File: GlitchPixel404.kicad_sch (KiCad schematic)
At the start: 61 parts, among them J1 USB_C_Receptacle_USB2.0_16P, J2 VOLTLINK, J5 Barrel_Jack_Switch, J7 Output, Q1 AONR21357-ES, Q2 MMBT3904, SW1 Reset, SW2 Boot, SW3 SW_SP3T, SW4 USER, U1 ESP32-PICO-MINI-02U-N8R2, U2 TPS54202DDC, U3 CH224K, U4 CH340N, U5 IRM-H6xxT, U6 74LVC2G34, U7 HE2021A50HMR, U8 74LVC2G34

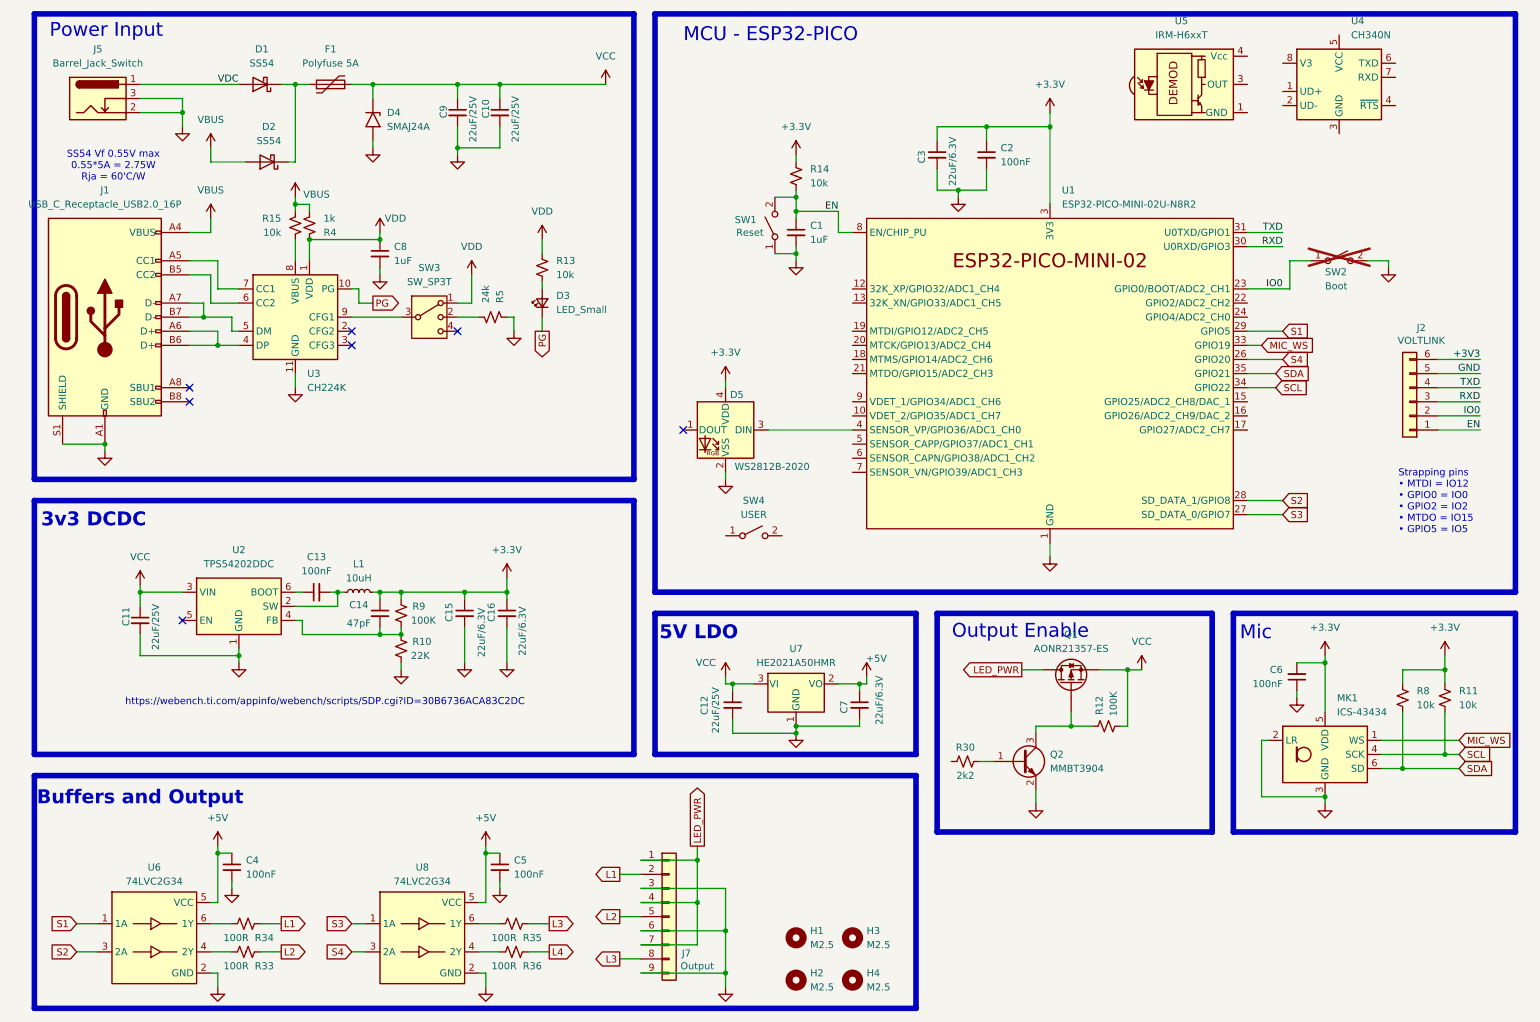
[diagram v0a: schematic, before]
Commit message: Added fet protection and started layout
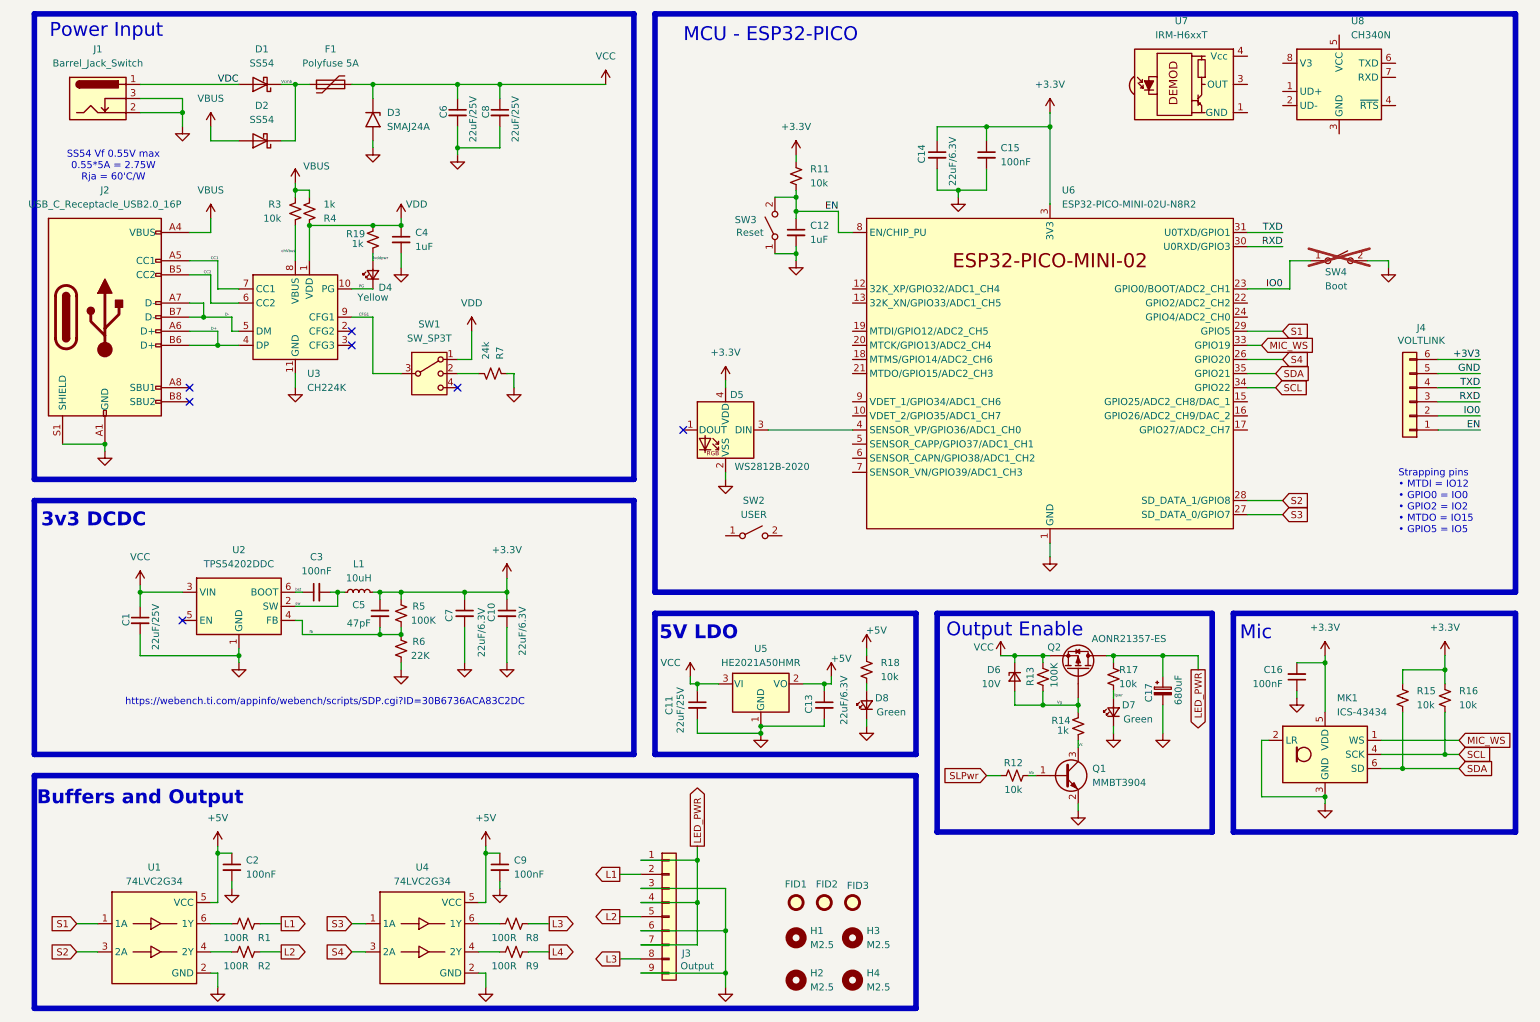
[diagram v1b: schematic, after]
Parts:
- removed R13: 10k, Resistor_SMD:R_0402_1005Metric, symbol Device:R_Small_US
- removed R30: 2k2, Resistor_SMD:R_0603_1608Metric, symbol Device:R_Small_US
- added C17: 680uF, Capacitor_SMD:CP_Elec_10x12.5, symbol Device:C_Polarized_Small
- added D6: 10V, Diode_SMD:D_SOD-123, symbol Device:D_Zener_Small
- added D7, D8: Green, LED_SMD:LED_0603_1608Metric, symbol Device:LED_Small
- added FID1, FID2, FID3: Fiducial, Fiducial:Fiducial_1mm_Mask2mm, symbol Mechanical:Fiducial
- added R12, R17, R18: 10k, Resistor_SMD:R_0402_1005Metric, symbol Device:R_Small_US
- added R14, R19: 1k, Resistor_SMD:R_0402_1005Metric, symbol Device:R_Small_US
- D4: renamed from D3; value LED_Small -> Yellow; LCSC (none) -> C72038; MPN (none) -> 19-213/Y2C-CQ2R2L/3T(CY)
- renumbered C11 to C1, C16 to C10, C12 to C11, C1 to C12, C7 to C13, C3 to C14, C2 to C15, C6 to C16, C4 to C2, C13 to C3, C8 to C4, C14 to C5, C9 to C6, C15 to C7, C10 to C8, C5 to C9, D4 to D3, J5 to J1, J1 to J2, J7 to J3, J2 to J4, Q2 to Q1, Q1 to Q2, R34 to R1, R14 to R11, R12 to R13, R8 to R15, R11 to R16, R33 to R2, R15 to R3, R9 to R5, R10 to R6, R5 to R7, R35 to R8, R36 to R9, SW3 to SW1, SW4 to SW2, SW1 to SW3, SW2 to SW4, U6 to U1, U8 to U4, U7 to U5, U1 to U6, U5 to U7, U4 to U8
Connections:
- net +5V: now also R18.1
- net GND: now also C17.2, D7.1 (K), D8.1 (K)
- net LED_PWR: now also C17.1, R17.1
- net VCC: now also D6.1 (K)
- net VDD: now also R19.2
- net Vg: now reaches Q2.G, R13.1
- net Vg: now also D6.2 (A), R14.2; no longer Q1.3 (C)
- net lvddpwr: now reaches D4.2 (A)
- net lvddpwr: now also R19.1
- net fb: now reaches C5.2, R5.2, R6.1, U2.4 (FB)
- net sw: now reaches C3.2, L1.1, U2.2 (SW)
- net bst: now reaches C3.1, U2.6 (BOOT)
- net CC1: now reaches J2.A5 (CC1), U3.7 (CC1)
- net D+: now reaches J2.A6 (D+), J2.B6 (D+), U3.4 (DP)
- net D-: now reaches J2.A7 (D-), J2.B7 (D-), U3.5 (DM)
- net CC2: now reaches J2.B5 (CC2), U3.6 (CC2)
- net Vb: now reaches Q1.1 (B)
- net Vb: now also R12.2
- net CFG1: now reaches SW1.3, U3.9 (CFG1)
- net Vcmb: now reaches D1.1 (K), D2.1 (K), F1.1
- net chVbus: now reaches R3.2, U3.8 (VBUS)
- new net: D8.2 (A), R18.2
- new net SLPwr: R12.1
- new net Vc: Q1.3 (C), R14.1
- new net llpwr: D7.2 (A), R17.2
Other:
- moved on the sheet: C11, C13, C4, D2, D4, Q1, Q2, R13, R3, R4, R7, SW1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

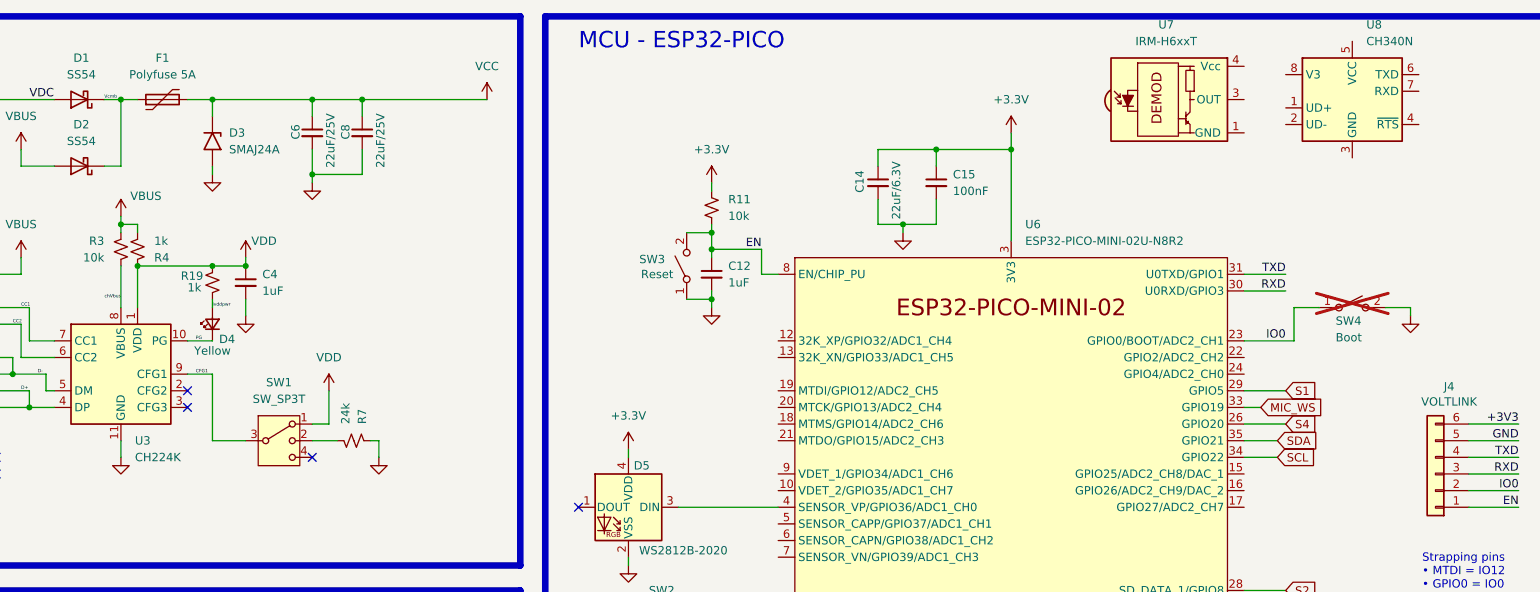
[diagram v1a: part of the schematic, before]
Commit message: remove CH340 and start layout
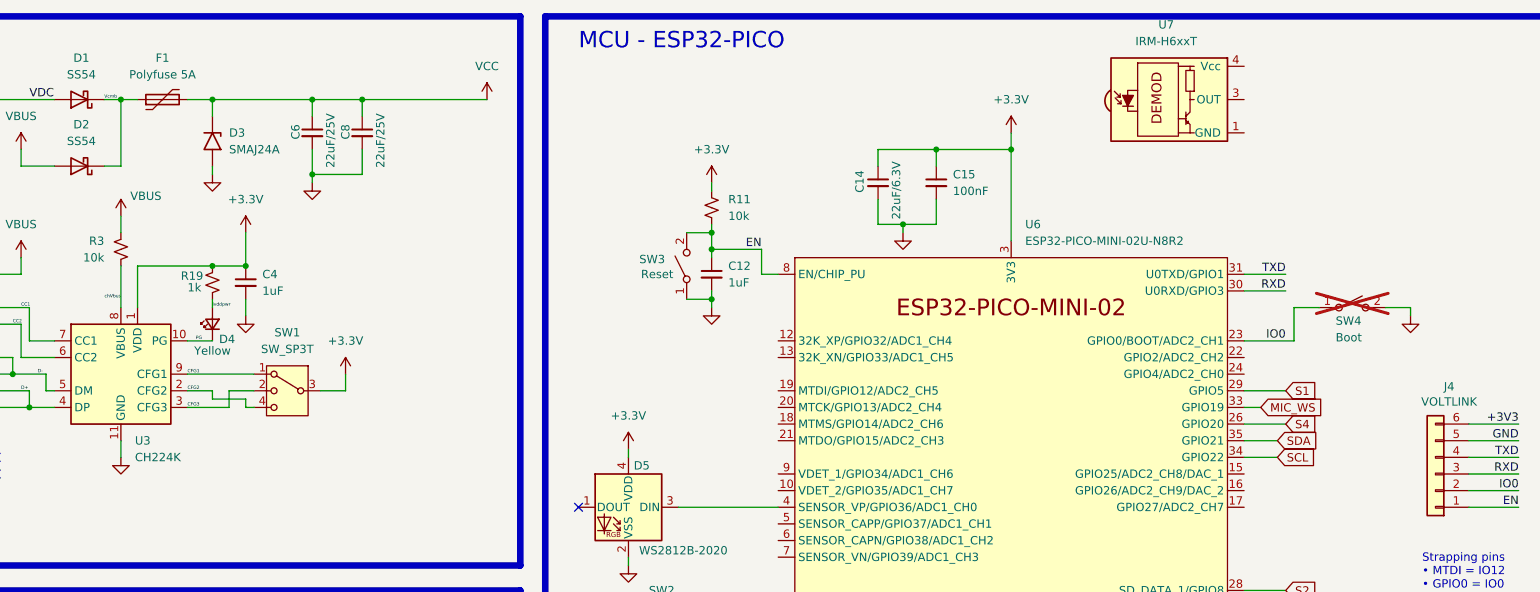
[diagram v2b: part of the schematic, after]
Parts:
- removed R4: 1k, Resistor_SMD:R_0402_1005Metric, symbol Device:R_Small_US
- removed R7: 24k, Resistor_SMD:R_0603_1608Metric, symbol Device:R_Small_US
- removed U8: CH340N, Package_SO:SOP-8_3.9x4.9mm_P1.27mm, symbol Interface_USB:CH340N
- SW4: now in the parts list
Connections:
- net +3.3V: now also C4.1, R19.2, SW1.3, U3.1 (VDD)
- net CFG1: now also SW1.1; no longer SW1.3
- net CFG3: now reaches SW1.2
- net CFG3: now also U3.3 (CFG3)
- net CFG2: now reaches SW1.4
- net CFG2: now also U3.2 (CFG2)
- removed net VDD: C4.1, R19.2, SW1.1, U3.1 (VDD)
- no-connect marks 7 -> 4
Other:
- moved on the sheet: SW1

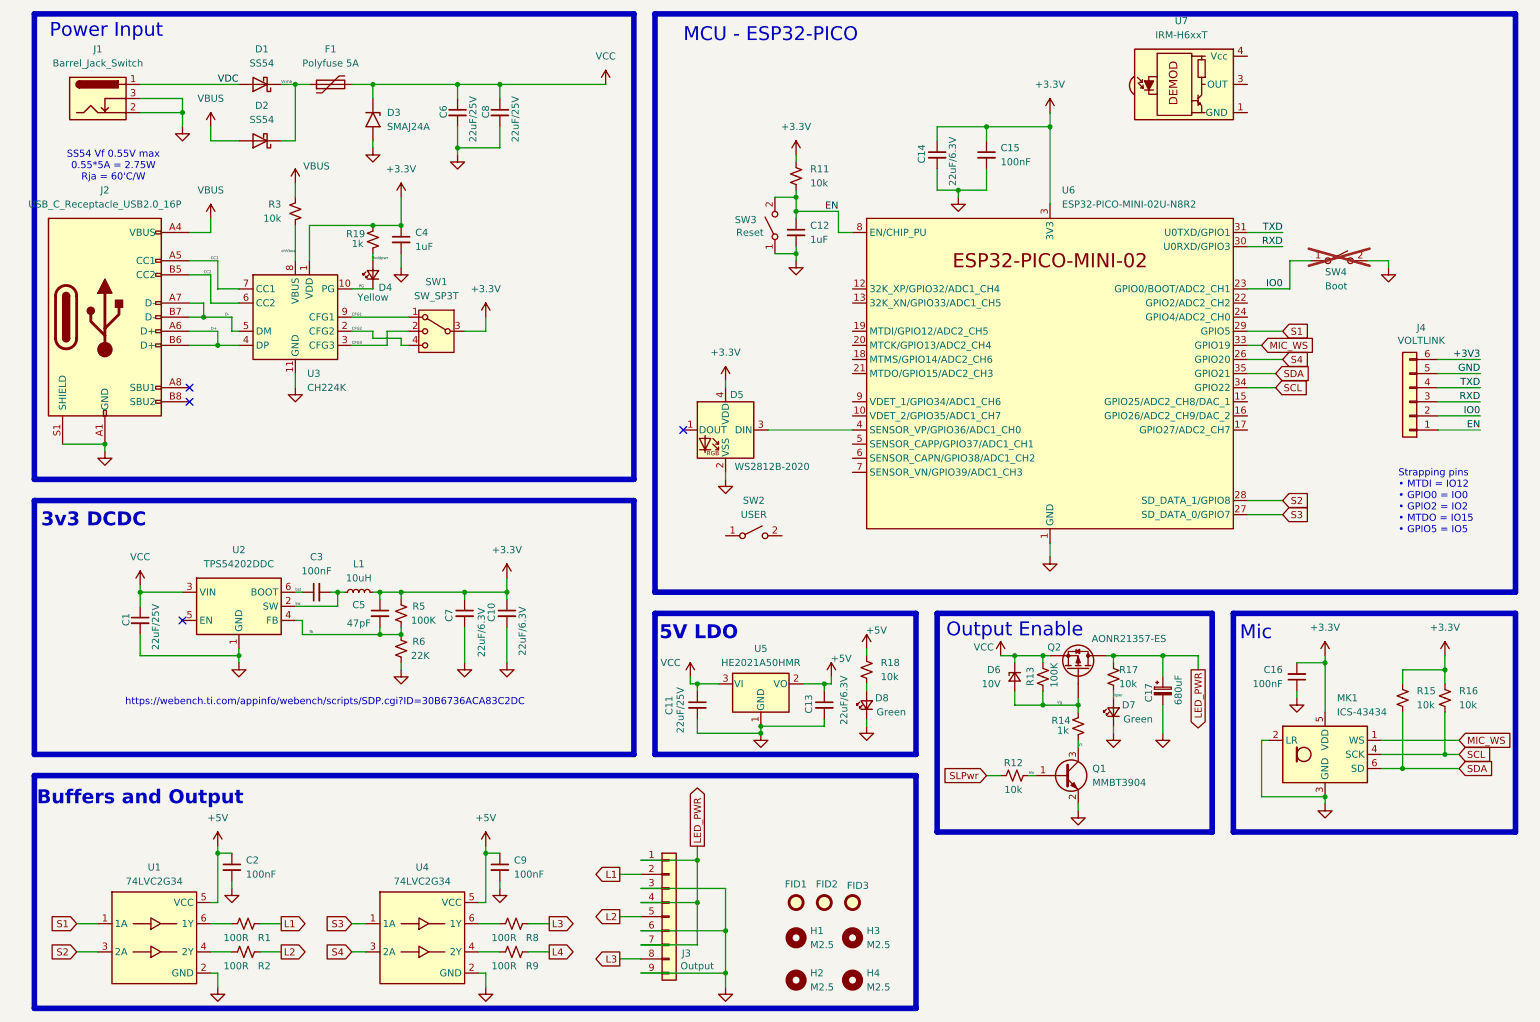
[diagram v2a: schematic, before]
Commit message: Layout 80% complete, some circuit changes
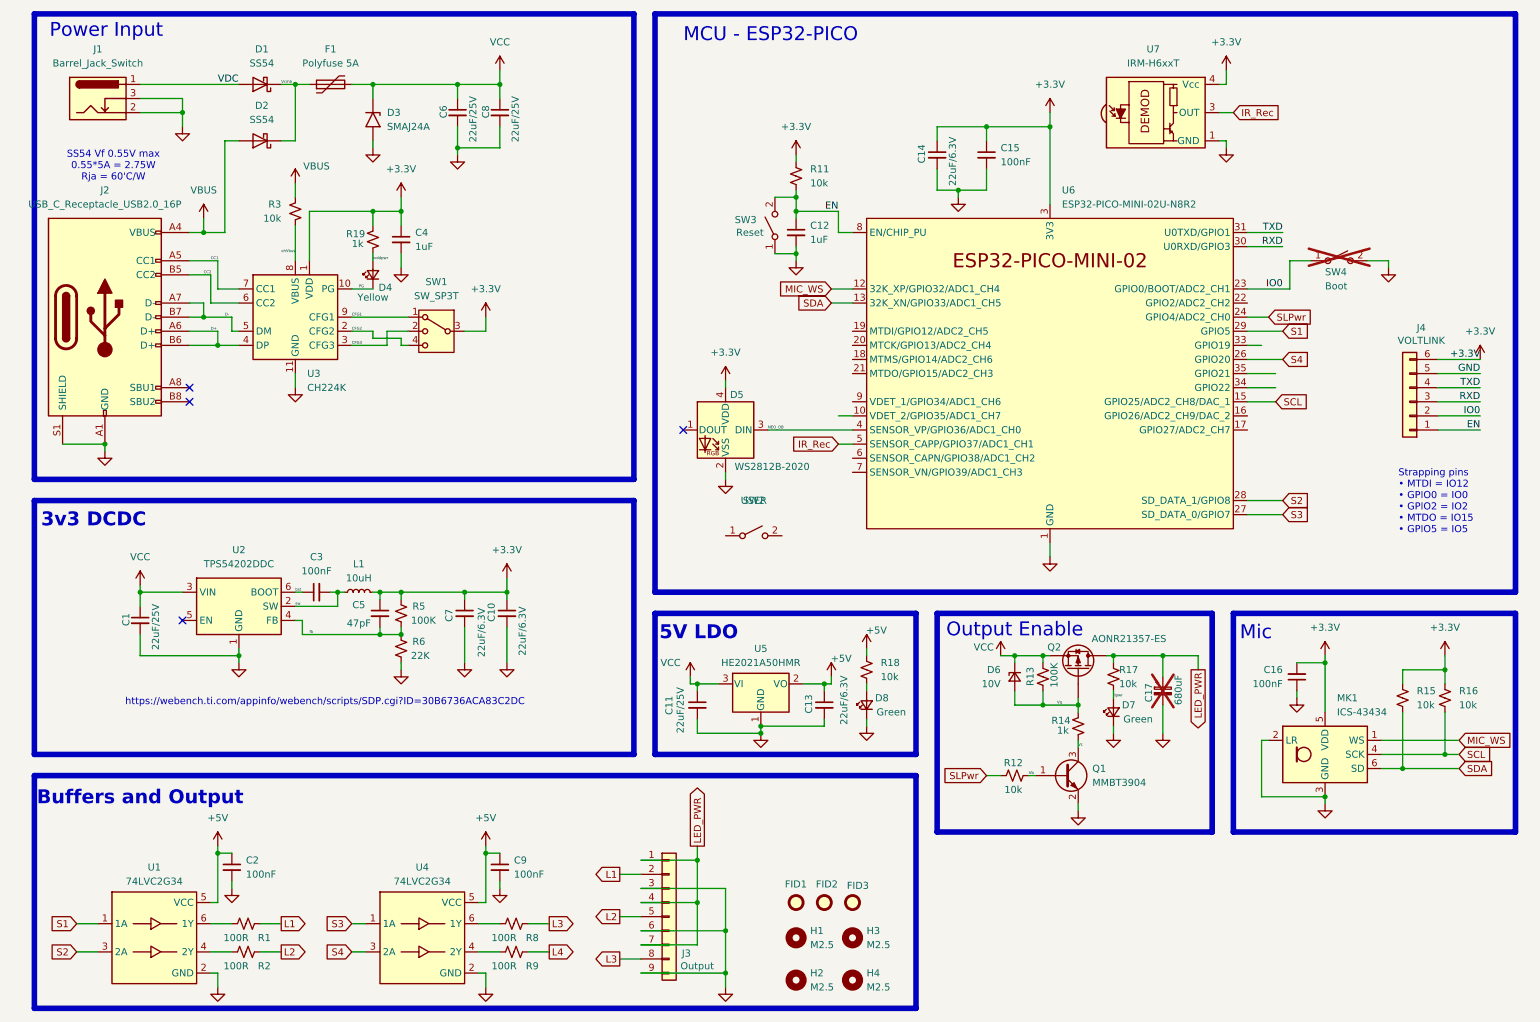
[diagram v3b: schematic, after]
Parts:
- C17: now not fitted; now left out of the parts list
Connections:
- net +3V3 is gone; now on net +3.3V: J4.6 (Pin_6)
- net +3.3V: now also U7.4 (Vcc)
- net GND: now also U7.1 (GND), U7.2 (GND)
- net MIC_WS: now also U6.12 (32K_XP/GPIO32/ADC1_CH4); no longer U6.33 (GPIO19)
- net SCL: now also U6.15 (GPIO25/ADC2_CH8/DAC_1); no longer U6.34 (GPIO22)
- net SDA: now also U6.13 (32K_XN/GPIO33/ADC1_CH5); no longer U6.35 (GPIO21)
- net SLPwr: now also U6.24 (GPIO4/ADC2_CH0)
- net IR_Rec: now reaches U7.3 (OUT)
- net IR_Rec: now also U6.5 (SENSOR_CAPP/GPIO37/ADC1_CH1)
- net NEO_OB: now reaches D5.3 (DIN), U6.4 (SENSOR_VP/GPIO36/ADC1_CH0)
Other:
- moved on the sheet: U7

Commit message: Minor corrections, silk started
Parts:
- removed C9: 100nF, Capacitor_SMD:C_0402_1005Metric, symbol Device:C_Small
- removed SW2: USER, symbol Switch:SW_SPST
- added D9: Yellow, LED_SMD:LED_0603_1608Metric, symbol Device:LED_Small
- added J5: Conn_01x03, Connector_PinHeader_2.54mm:PinHeader_1x03_P2.54mm_Vertical, symbol Connector_Generic:Conn_01x03
- added R20: 10k, Resistor_SMD:R_0402_1005Metric, symbol Device:R_Small_US
- SW4: now fitted
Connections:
- net +3.3V: now also R20.1
- net GND: now also D9.1 (K), J5.3 (Pin_3)
- net L4: now also J5.2 (Pin_2)
- net LED_PWR: now also J5.1 (Pin_1)
- new net: D9.2 (A), R20.2
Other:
- moved on the sheet: C11, C13, C2, D8, R18, U5
